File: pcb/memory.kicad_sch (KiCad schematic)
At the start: 3 parts, among them U7 MT41K256M16LY, U8 MX25L3233FZN

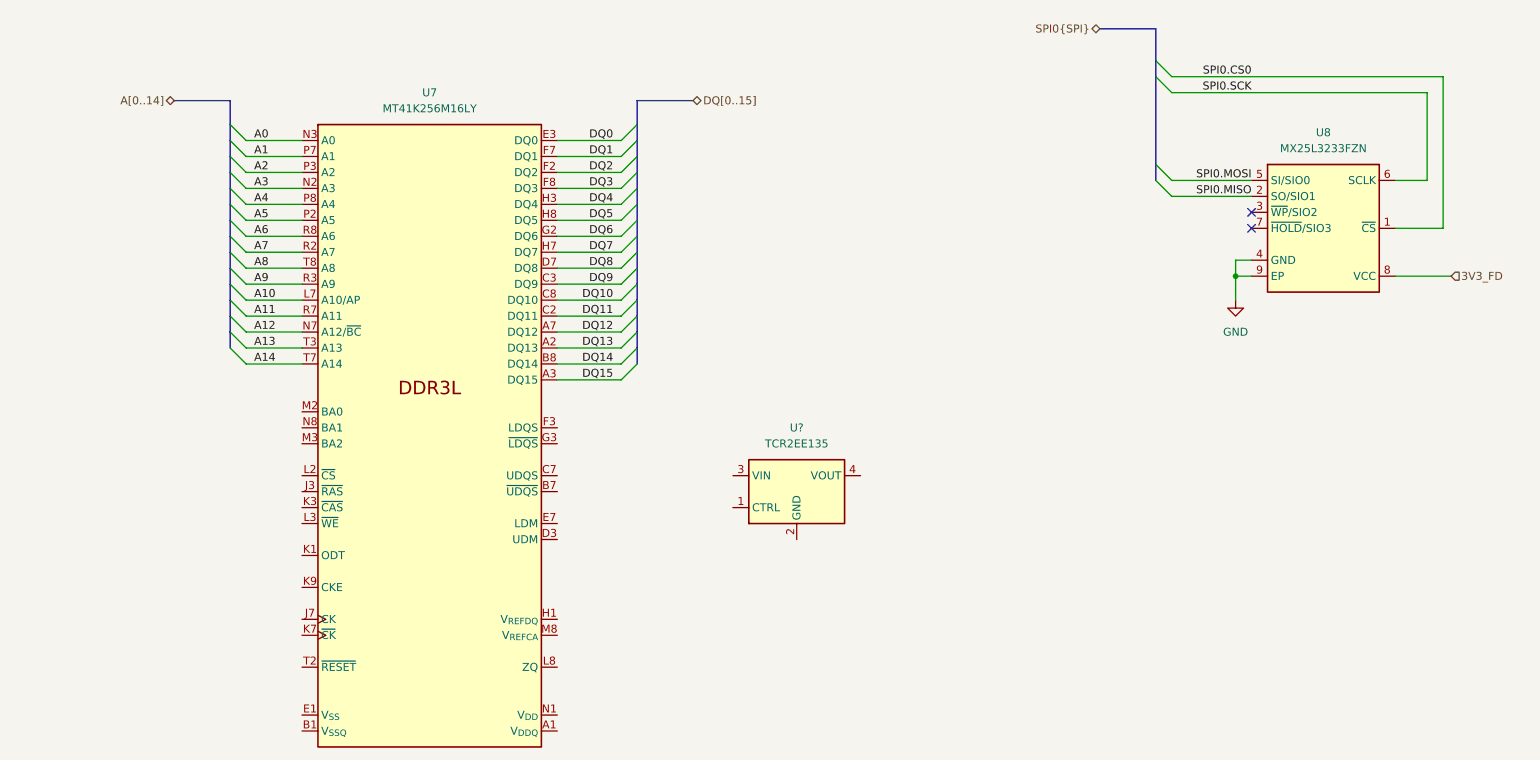
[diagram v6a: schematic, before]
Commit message: defined memory pinouts
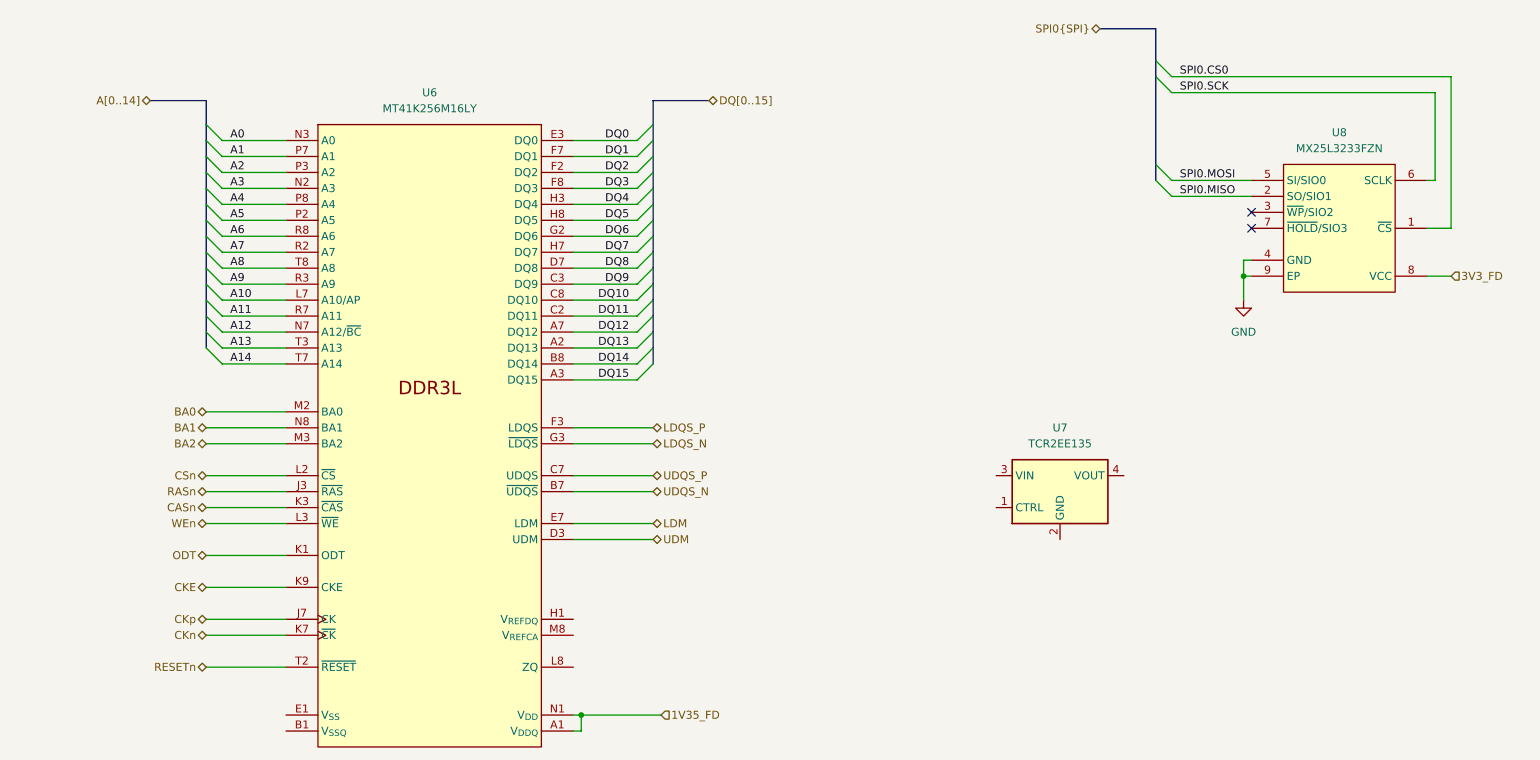
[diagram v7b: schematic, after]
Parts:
- gave numbers to parts that had none: 1
- renumbered U7 to U6
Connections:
- net 1V35_FD: now reaches U6.A1 (V_{DDQ})
- net 1V35_FD: now also U6.A8 (V_{DDQ}), U6.B2 (V_{DD}), U6.C1 (V_{DDQ}), U6.C9 (V_{DDQ}), U6.D2 (V_{DDQ}), U6.D9 (V_{DD}), U6.E9 (V_{DDQ}), U6.F1 (V_{DDQ}), U6.G7 (V_{DD}), U6.H2 (V_{DDQ}), U6.H9 (V_{DDQ}), U6.K2 (V_{DD}), U6.K8 (V_{DD}), U6.N1 (V_{DD}), U6.N9 (V_{DD}), U6.R1 (V_{DD}), U6.R9 (V_{DD})
- net at U6.A9 (V_{SS}), U6.B3 (V_{SS}), U6.G8 (V_{SS})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: now also U6.E1 (V_{SS})
- net at U6.B1 (V_{SSQ}): now also U6.B9 (V_{SSQ}), U6.D1 (V_{SSQ}), U6.D8 (V_{SSQ}), U6.E2 (V_{SSQ}), U6.E8 (V_{SSQ}), U6.F9 (V_{SSQ}), U6.G1 (V_{SSQ}), U6.G9 (V_{SSQ})
- net UDQS_N: now reaches U6.B7 (~{UDQS})
- net UDQS_P: now reaches U6.C7 (UDQS)
- net UDM: now reaches U6.D3 (UDM)
- net LDM: now reaches U6.E7 (LDM)
- net LDQS_P: now reaches U6.F3 (LDQS)
- net LDQS_N: now reaches U6.G3 (~{LDQS})
- net RASn: now reaches U6.J3 (~{RAS})
- net CKp: now reaches U6.J7 (CK)
- net ODT: now reaches U6.K1 (ODT)
- net CASn: now reaches U6.K3 (~{CAS})
- net CKn: now reaches U6.K7 (~{CK})
- net CKE: now reaches U6.K9 (CKE)
- net CSn: now reaches U6.L2 (~{CS})
- net WEn: now reaches U6.L3 (~{WE})
- net BA0: now reaches U6.M2 (BA0)
- net BA2: now reaches U6.M3 (BA2)
- net BA1: now reaches U6.N8 (BA1)
- net RESETn: now reaches U6.T2 (~{RESET})
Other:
- moved on the sheet: U7, U8

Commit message: power restructuring
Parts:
- removed U7: TCR2EE135, Package_TO_SOT_SMD:SOT-553, symbol library:TCR2EE135
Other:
- moved on the sheet: U8
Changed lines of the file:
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@@
 	)
 	(no_connect
-		(at 237.49 58.42)
+		(at 238.76 58.42)
 	)
 	(no_connect
-		(at 237.49 55.88)
+		(at 238.76 55.88)
 	)
 	(bus_entry
@@
 	)
 	(bus_entry
-		(at 222.25 48.26)
+		(at 220.98 48.26)
 		(size 2.54 2.54)
 		(stroke
@@
 	)
 	(bus_entry
-		(at 222.25 31.75)
+		(at 220.98 31.75)
 		(size 2.54 2.54)
 		(stroke
@@
 	)
 	(bus_entry
-		(at 222.25 50.8)
+		(at 220.98 50.8)
 		(size 2.54 2.54)
 		(stroke
@@
 	)
 	(bus_entry
-		(at 222.25 34.29)
+		(at 220.98 34.29)
 		(size 2.54 2.54)
 		(stroke
@@
 	(bus
 		(pts
-			(xy 222.25 48.26) (xy 222.25 50.8)
+			(xy 220.98 48.26) (xy 220.98 50.8)
 		)
 		(stroke
@@
 	(bus
 		(pts
-			(xy 222.25 26.67) (xy 222.25 31.75)
+			(xy 220.98 25.4) (xy 220.98 31.75)
 		)
 		(stroke
@@
 	(wire
 		(pts
-			(xy 269.24 34.29) (xy 269.24 58.42)
+			(xy 271.78 34.29) (xy 271.78 58.42)
 		)
 		(stroke
@@
 	(wire
 		(pts
-			(xy 224.79 50.8) (xy 237.49 50.8)
+			(xy 223.52 50.8) (xy 238.76 50.8)
 		)
 		(stroke
@@
 	(wire
 		(pts
-			(xy 224.79 53.34) (xy 237.49 53.34)
-		)
-		(stroke
-			(width 0)
-			(type default)
-		)
-	)
-	(wire
-		(pts
-			(xy 266.7 50.8) (xy 265.43 50.8)
+			(xy 223.52 53.34) (xy 238.76 53.34)
 		)
 		(stroke
@@
 	(wire
 		(pts
-			(xy 237.49 63.5) (xy 236.22 63.5)
+			(xy 238.76 63.5) (xy 236.22 63.5)
 		)
 		(stroke
@@
 	(wire
 		(pts
-			(xy 266.7 36.83) (xy 266.7 50.8)
+			(xy 269.24 36.83) (xy 269.24 50.8)
 		)
 		(stroke
@@
 	(wire
 		(pts
-			(xy 265.43 66.04) (xy 269.24 66.04)
-		)
-		(stroke
-			(width 0)
-			(type default)
-		)
-	)
-	(wire
-		(pts
-			(xy 236.22 66.04) (xy 237.49 66.04)
+			(xy 266.7 66.04) (xy 271.78 66.04)
+		)
+		(stroke
+			(width 0)
+			(type default)
+		)
+	)
+	(wire
+		(pts
+			(xy 236.22 66.04) (xy 238.76 66.04)
 		)
 		(stroke
@@
 	(wire
 		(pts
-			(xy 224.79 36.83) (xy 266.7 36.83)
+			(xy 223.52 36.83) (xy 269.24 36.83)
 		)
 		(stroke
@@
 	(bus
 		(pts
-			(xy 213.36 26.67) (xy 222.25 26.67)
-		)
-		(stroke
-			(width 0)
-			(type default)
-		)
-	)
-	(bus
-		(pts
-			(xy 222.25 34.29) (xy 222.25 48.26)
+			(xy 213.36 25.4) (xy 220.98 25.4)
+		)
+		(stroke
+			(width 0)
+			(type default)
+		)
+	)
+	(bus
+		(pts
+			(xy 220.98 34.29) (xy 220.98 48.26)
 		)
 		(stroke
@@
 	(wire
 		(pts
-			(xy 265.43 58.42) (xy 269.24 58.42)
+			(xy 266.7 58.42) (xy 271.78 58.42)
 		)
 		(stroke
@@
 	(bus
 		(pts
-			(xy 222.25 31.75) (xy 222.25 34.29)
+			(xy 220.98 31.75) (xy 220.98 34.29)
 		)
 		(stroke
@@
 	(wire
 		(pts
-			(xy 224.79 34.29) (xy 269.24 34.29)
+			(xy 269.24 50.8) (xy 266.7 50.8)
+		)
+		(stroke
+			(width 0)
+			(type default)
+		)
+	)
+	(wire
+		(pts
+			(xy 223.52 34.29) (xy 271.78 34.29)
 		)
 		(stroke
@@
 	(hierarchical_label "SPI0{SPI}"
 		(shape bidirectional)
-		(at 213.36 26.67 180)
+		(at 213.36 25.4 180)
 		(effects
 			(font
@@
 	(hierarchical_label "3V3_FD"
 		(shape input)
-		(at 269.24 66.04 0)
+		(at 271.78 66.04 0)
 		(effects
 			(font
@@
 	(symbol
 		(lib_id "library:MX25L3233FZN")
-		(at 251.46 58.42 0)
+		(at 252.73 58.42 0)
 		(unit 1)
 		(exclude_from_sim no)
@@
 		(fields_autoplaced yes)
 		(property "Reference" "U8"
-			(at 251.46 43.18 0)
+			(at 252.73 43.18 0)
 			(effects
 				(font
@@
 		)
 		(property "Value" "MX25L3233FZN"
-			(at 251.46 45.72 0)
+			(at 252.73 45.72 0)
 			(effects
 				(font
@@
 		)
 		(property "Footprint" "Package_SON:WSON-8-1EP_6x5mm_P1.27mm_EP3.4x4mm"
-			(at 251.46 73.66 0)
+			(at 252.73 73.66 0)
 			(effects
 				(font
@@
 		)
 		(property "Datasheet" "https://www.macronix.com/Lists/Datasheet/Attachments/8377/MX25L3233F,%203V,%2032Mb,%20v1.1.pdf"
-			(at 251.46 75.946 0)
+			(at 252.73 75.946 0)
 			(effects
 				(font
@@
 		)
 		(property "Description" "32-Mbit, 3V (2.65V-3.6V) SPI Serial Flash Memory, WSON-8"
-			(at 250.19 58.42 0)
-			(effects
-				(font
-					(size 1.27 1.27)
-				)
-				(hide yes)
-			)
-		)
-		(property "Name" ""
 			(at 251.46 58.42 0)
 			(effects
@@
 			)
 		)
+		(property "Name" ""
+			(at 252.73 58.42 0)
+			(effects
+				(font
+					(size 1.27 1.27)
+				)
+				(hide yes)
+			)
+		)
 		(pin "4"
 		)
@@
 					(unit 1)
 				)
-			)
-		)
-	)
-	(symbol
-		(lib_id "library:TCR2EE135")
-		(at 207.01 100.33 0)
-		(unit 1)
-		(exclude_from_sim no)
-		(in_bom yes)
-		(on_board yes)
-		(dnp no)
-		(fields_autoplaced yes)
-		(property "Reference" "U7"
-			(at 207.01 90.17 0)
-			(effects
-				(font
-					(size 1.27 1.27)
-				)
-			)
-		)
-		(property "Value" "TCR2EE135"
-			(at 207.01 92.71 0)
-			(effects
-				(font
-					(size 1.27 1.27)
-				)
-			)
-		)
-		(property "Footprint" "Package_TO_SOT_SMD:SOT-553"
-			(at 207.01 110.49 0)
-			(effects
-				(font
-					(size 1.27 1.27)
-				)
-				(hide yes)
-			)
-		)
-		(property "Datasheet" "https://toshiba.semicon-storage.com/info/docget.jsp?did=13794&prodName=TCR2EF45"
-			(at 200.66 93.98 0)
-			(effects
-				(font
-					(size 1.27 1.27)
-				)
-				(hide yes)
-			)
-		)
-		(property "Description" "200mA Low-dropout Voltage Regulator, Vout 1.35V, Vin up to 5.5V, SOT-553"
-			(at 207.01 100.33 0)
-			(effects
-				(font
-					(size 1.27 1.27)
-				)
-				(hide yes)
-			)
-		)
-		(property "Name" ""
-			(at 207.01 100.33 0)
-			(effects
-				(font
-					(size 1.27 1.27)
-				)
-				(hide yes)
-			)
-		)
-		(pin "5"
-		)
-		(pin "2"
-		)
-		(pin "1"
-		)
-		(pin "3"
-		)
-		(pin "4"
-		)
-		(instances
-			(project ""
-				(path "/e63e39d7-6ac0-4ffd-8aa3-1841a4541b55/59d21473-a004-4514-8090-fd93db818925/b633a666-4c3d-4ac9-9e0f-b350177ade0b"
-					(reference "U7")
-					(unit 1)
-				)
